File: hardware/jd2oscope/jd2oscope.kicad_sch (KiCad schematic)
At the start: 0 parts

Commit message: feat: kicad board dev
parts added, general framework established
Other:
- removed sheet Touchscreen
- removed sheet UserInteractionInterface
- added sheet ADCModule (ADCModule.kicad_sch)
- added sheet Touchscreen_LCD_Display (Touchscreen_LCD_Display.kicad_sch)
- added sheet buttonModule (buttonModule.kicad_sch)
- added sheet potentiometerModule (PotentiometerModule.kicad_sch)
- added sheet switchModule (switchModule.kicad_sch)
- note added: "(GPIO 18)"
- note added: "(GPIO 19)"
- note added: "(GPIO 23)"
- note added: "(any; GPIO 15)"
- note added: "(any; GPIO 2)"
- note added: "(any; GPIO 27)"
- note added: "(any; GPIO 5)"

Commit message: fix: pushing so people can edit!! (I think)
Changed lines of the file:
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@@
+		)
+	)
+	(hierarchical_label "screen_SDO"
+		(shape output)
+		(at 50.8 99.06 0)
+		(effects
+			(font
+				(size 1.27 1.27)
+			)
+			(justify left)
+		)
+	)
+	(hierarchical_label "5V"
+		(shape input)
+		(at 30.48 127 270)
+		(effects
+			(font
+				(size 1.27 1.27)
+			)
+			(justify right)
+		)
+	)
+	(hierarchical_label "screen_CS"
+		(shape input)
+		(at 50.8 83.82 0)
+		(effects
+			(font
+				(size 1.27 1.27)
+			)
+			(justify left)
+		)
+	)
+	(hierarchical_label "3.3V"
+		(shape input)
+		(at 33.02 127 270)
+		(effects
+			(font
+				(size 1.27 1.27)
+			)
+			(justify right)
+		)
+	)
+	(hierarchical_label "screen_SCK"
+		(shape input)
+		(at 50.8 95.25 0)
+		(effects
+			(font
+				(size 1.27 1.27)
+			)
+			(justify left)
+		)
+	)
+	(hierarchical_label "screen_T_IRQ"
+		(shape output)
+		(at 50.8 120.65 0)
+		(effects
+			(font
+				(size 1.27 1.27)
+			)
+			(justify left)
+		)
+	)
+	(hierarchical_label "screen_T_CS"
+		(shape input)
+		(at 50.8 109.22 0)
+		(effects
+			(font
+				(size 1.27 1.27)
+			)
+			(justify left)
+		)
+	)
+	(hierarchical_label "screen_T_DIN"
+		(shape input)
+		(at 50.8 113.03 0)
+		(effects
+			(font
+				(size 1.27 1.27)
+			)
+			(justify left)
+		)
+	)
+	(hierarchical_label "screen_T_DO"
+		(shape output)
+		(at 50.8 116.84 0)
+		(effects
+			(font
+				(size 1.27 1.27)
+			)
+			(justify left)
+		)
+	)
+	(hierarchical_label "screen_T_CLK"
+		(shape input)
+		(at 50.8 105.41 0)
+		(effects
+			(font
+				(size 1.27 1.27)
+			)
+			(justify left)
+		)
+	)
+	(hierarchical_label "screen_SDI"
+		(shape input)
+		(at 50.8 91.44 0)
+		(effects
+			(font
+				(size 1.27 1.27)
+			)
+			(justify left)
+		)
+	)
+	(hierarchical_label "screen_D{slash}C"
+		(shape input)
+		(at 50.8 87.63 0)
+		(effects
+			(font
+				(size 1.27 1.27)
+			)
+			(justify left)
+		)
+	)
+	(symbol
+		(lib_id "power:GND")
+		(at 50.8 125.73 90)
+		(unit 1)
+		(exclude_from_sim no)
+		(in_bom yes)
+		(on_board yes)
+		(dnp no)
+		(fields_autoplaced yes)
+		(property "Reference" "#PWR01"
+			(at 57.15 125.73 0)
+			(effects
+				(font
+					(size 1.27 1.27)
+				)
+				(hide yes)
+			)
+		)
+		(property "Value" "GND"
+			(at 54.61 125.7299 90)
+			(effects
+				(font
+					(size 1.27 1.27)
+				)
+				(justify right)
+			)
+		)
+		(property "Footprint" ""
+			(at 50.8 125.73 0)
+			(effects
+				(font
+					(size 1.27 1.27)
+				)
+				(hide yes)
+			)
+		)
+		(property "Datasheet" ""
+			(at 50.8 125.73 0)
+			(effects
+				(font
+					(size 1.27 1.27)
+				)
+				(hide yes)
+			)
+		)
+		(property "Description" "Power symbol creates a global label with name \"GND\" , ground"
+			(at 50.8 125.73 0)
+			(effects
+				(font
+					(size 1.27 1.27)
+				)
+				(hide yes)
+			)
+		)
+		(pin "1"
+		)
+		(instances
+			(project ""
+				(path "/eb18a3da-9fbf-4329-a814-1afab785c817"
+					(reference "#PWR01")
+					(unit 1)
+				)
+			)
 		)
 	)
@@
 	)
 	(sheet
-		(at 97.79 144.78)
-		(size 17.78 16.51)
+		(at 97.79 123.19)
+		(size 17.78 38.1)
 		(fields_autoplaced yes)
 		(stroke
@@
 		)
 		(property "Sheetname" "ESP32"
-			(at 97.79 144.0684 0)
-			(effects
-				(font
+			(at 97.79 122.4784 0)
+			(effects
+				(font

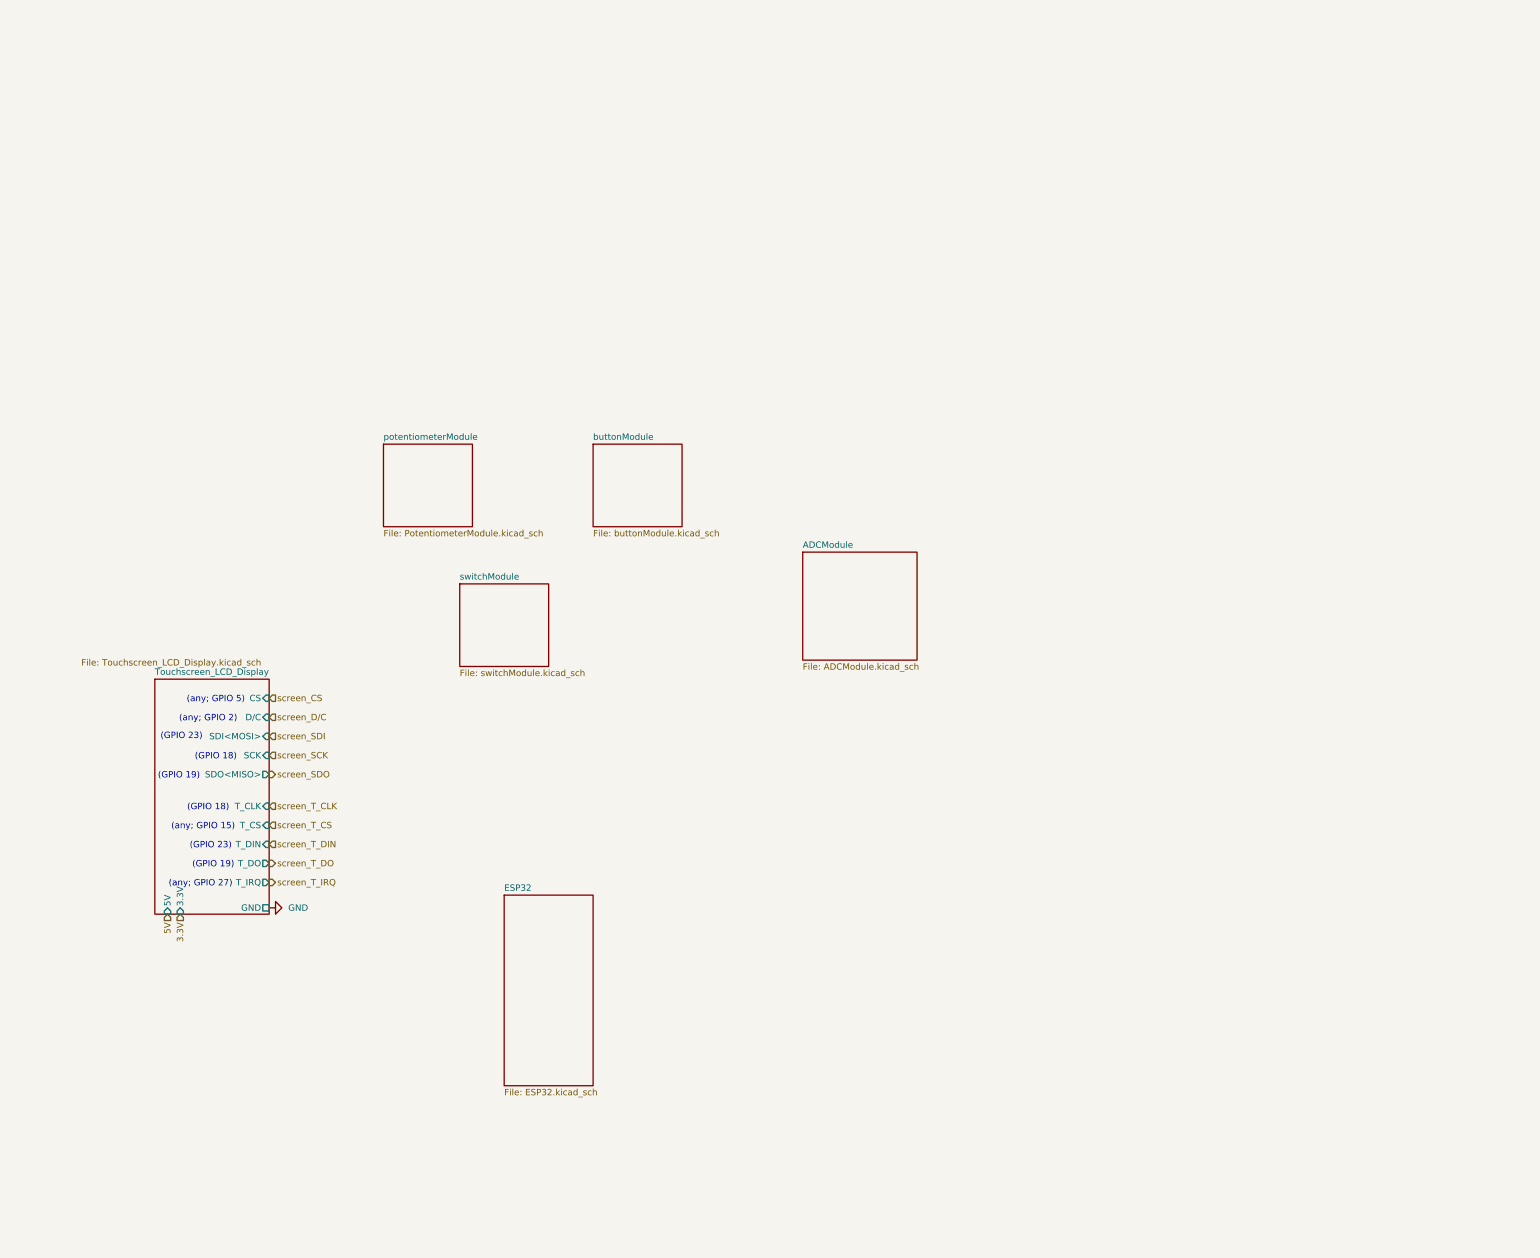
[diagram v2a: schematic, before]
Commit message: feat: screen implemented
alongside screen implementation, re-structured layout for schematics, and cleaned up SPI comm. conn.s; also implemented ADC module successfully (sans SPI section for it; that comes next)
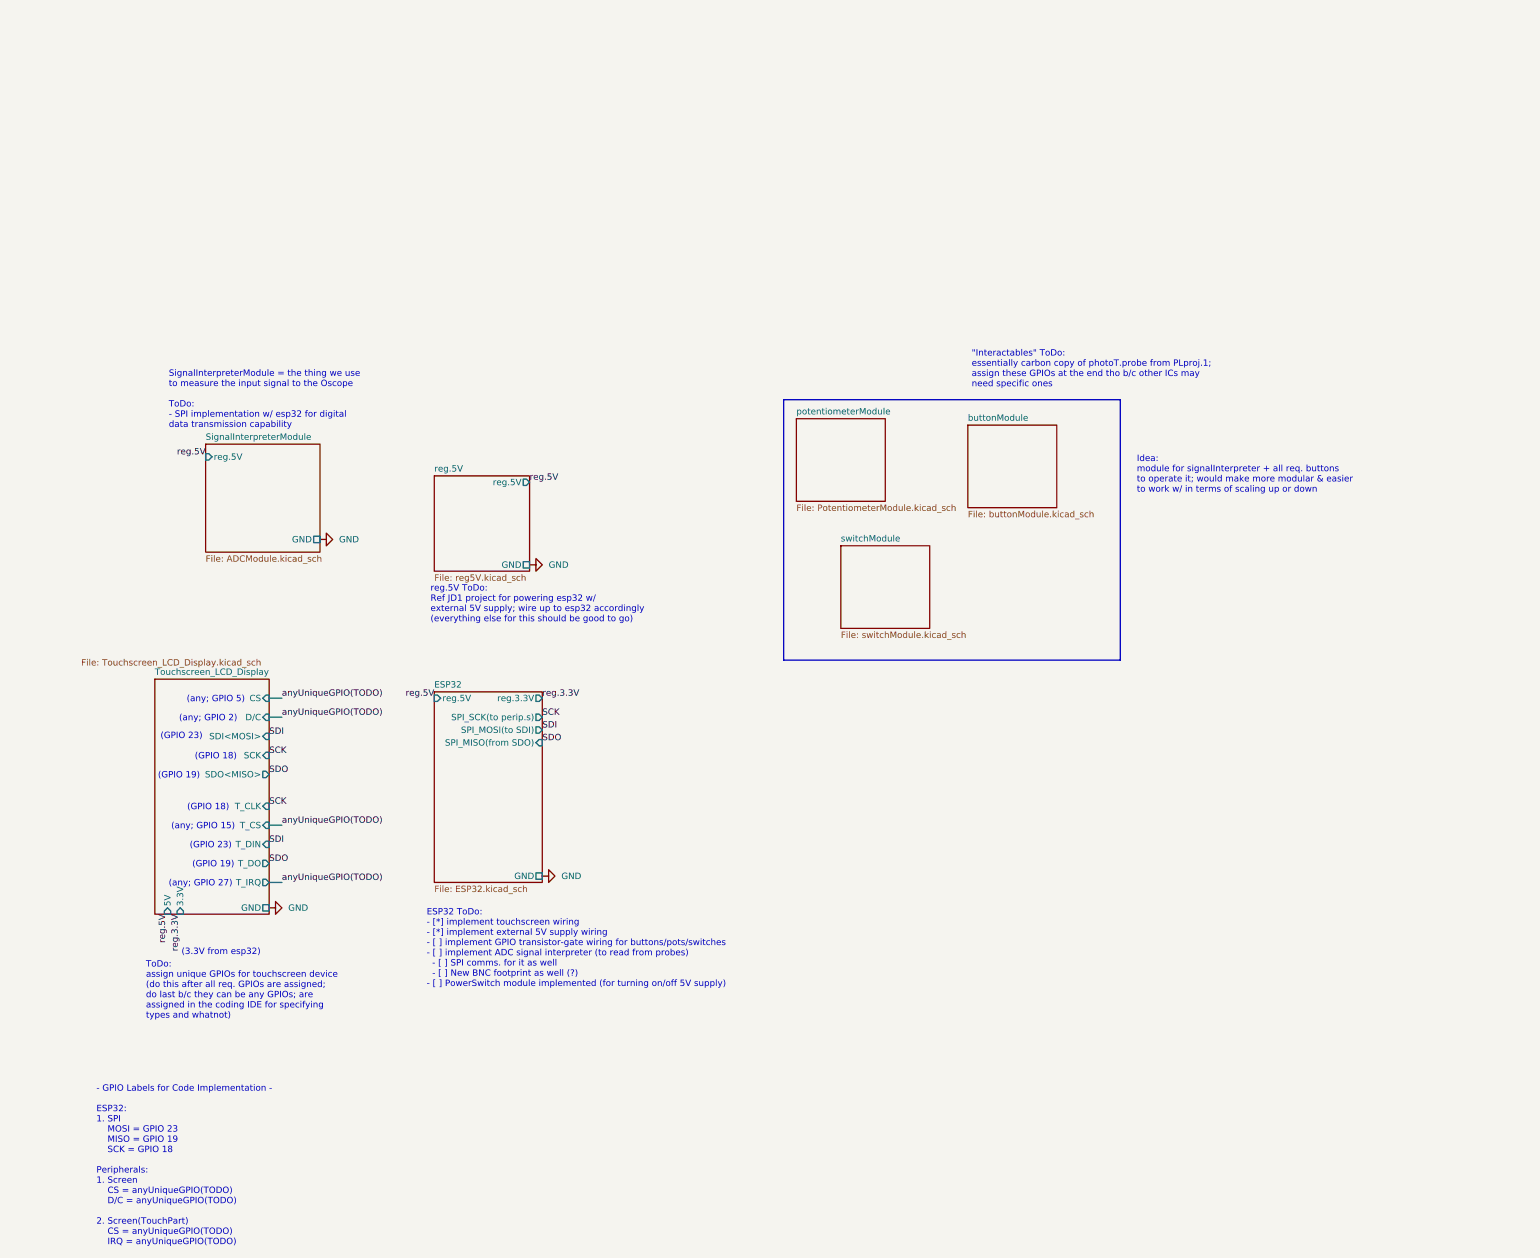
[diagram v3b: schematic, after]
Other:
- sheet ADCModule renamed SignalInterpreterModule
- added sheet reg.5V (reg5V.kicad_sch)
- sheet ESP32 ports: added GND, SPI_MISO(from SDO), SPI_MOSI(to SDI), SPI_SCK(to perip.s), reg.3.3V, reg.5V; removed none
- sheet SignalInterpreterModule ports: added GND, reg.5V; removed none
- note added: ""Interactables" ToDo: essentially carbon copy of photoT.probe from PLproj.1; assign these GPIOs at the end tho b/c other ICs may need specific ones"
- note added: "(3.3V from esp32)"
- note added: "- GPIO Labels for Code Implementation - ESP32: 1. SPI MOSI = GPIO 23 MISO = GPIO 19 SCK = GPIO 18 Peripherals: 1. Screen CS = anyUniqueGPIO(TODO) D/C = anyUniqueGPIO(TODO) 2. Screen(TouchPart) CS = anyUniqueGPIO(TODO) IRQ = anyUniqueGPIO(TODO)"
- note added: "ESP32 ToDo: - [*] implement touchscreen wiring - [*] implement external 5V supply wiring - [ ] implement GPIO transistor-gate wiring for buttons/pots/switches - [ ] implement ADC signal interpreter (to read from probes) - [ ] SPI comms. for it as well - [ ] New BNC footprint as well (?) - [ ] PowerSwitch module implemented (for turning on/off 5V supply)"
- note added: "Idea: module for signalInterpreter + all req. buttons to operate it; would make more modular & easier to work w/ in terms of scaling up or down"
- note added: "SignalInterpreterModule = the thing we use to measure the input signal to the Oscope ToDo: - SPI implementation w/ esp32 for digital data transmission capability"
- note added: "ToDo: assign unique GPIOs for touchscreen device (do this after all req. GPIOs are assigned; do last b/c they can be any GPIOs; are assigned in the coding IDE for specifying types and whatnot)"
- note added: "reg.5V ToDo: Ref JD1 project for powering esp32 w/ external 5V supply; wire up to esp32 accordingly (everything else for this should be good to go)"

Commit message: feat: lot of progress
added decoupling caps, implemented a lot more of the comm. protocol stuffs, updated BNC connector to updated version, added more notes for GPIO pin I/O for future code implementation, lot of other stuff too (frankly can't remember all of it lol); I commit here b/c want to back up progress b/4 I go get smth to eat ;)
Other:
- sheet reg.5V renamed 5V_Regulator
- removed sheet switchModule
- sheet SignalInterpreterModule ports: added ADC_CONVST, ADC_CS, ADC_EOC/INT, ADC_SCK, ADC_SDI, ADC_SDO; removed none
- sheet buttonModule ports: added GND, GPIOpin; removed none
- sheet potentiometerModule ports: added GND, POT_WIPER, reg.3.3V; removed none
- note added: "- GPIO Labels for Code Implementation - ESP32: 1. SPI MOSI = GPIO 23 MISO = GPIO 19 SCK = GPIO 18 Peripherals: 1. Screen(Display) S_CS = anyUniqueGPIO(TODO) D/C = anyUniqueGPIO(TODO) 2. Screen(Touchscreen Function) T_CS = anyUniqueGPIO(TODO) IRQ = anyUniqueGPIO(TODO) 3. ADC #1 ADC1_CS = anyUniqueGPIO(TODO) ADC1_CONVST = anyUniqueGPIO(TODO) ADC1_EOC/INT = anyUniqueGPIO(TODO) 4. ADC #2 ADC2_CS = an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"
- note added: "ESP32 Remaining Pinout ToDo: add arbitrary GPIO pins for all req. unique connections"
- note added: "ESP32 ToDo: - [*] implement touchscreen wiring - [*] implement 5V_Regulator - [*] PowerSwitch module between regulator output & reg.5V (for toggling reg.5V to all dependent perip.s (i.e. turning device on/off) - [ ] modules completed for: - [*] pot.s - [*] buttons - [ ] created "signalInterfaceModule"; has all req. buttons/pot.s to fully control 1x signal (like a "package" that has everything we 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"
- note added: "How many buttons & pot.s needed per "signal module"? - [ ] after determining, build signal module - [ ] try out hierarchecal pcb setup too(?) - compatability should be fine (?)"
- note added: "Remaining GPIOs: - [ ] for each of the potentiometers & buttons Helpful Note: - for GPIO groupings do this (ex): " Peripherals: SignalModule1: ADC1: ADC1_CS = (...) Button1 = (...) SignalModule2: (...) " ^Effectively, one "module" for e/a signal input; group e/a as a separate peripheral"
- note added: "SignalInterpreterModule = the module we use to measure a BNC input signal to the Oscope"
- note added: "ToDo: assign unique GPIOs for screen & TS perip.s (do this after all req. GPIOs are assigned; do last b/c they can be any GPIOs; are assigned in the coding IDE for specifying types and whatnot)"
- note removed: ""Interactables" ToDo: essentially carbon copy of photoT.probe from PLproj.1; assign these GPIOs at the end tho b/c other ICs may need specific ones"
- note removed: "(3.3V from esp32)"
- note removed: "- GPIO Labels for Code Implementation - ESP32: 1. SPI MOSI = GPIO 23 MISO = GPIO 19 SCK = GPIO 18 Peripherals: 1. Screen CS = anyUniqueGPIO(TODO) D/C = anyUniqueGPIO(TODO) 2. Screen(TouchPart) CS = anyUniqueGPIO(TODO) IRQ = anyUniqueGPIO(TODO)"
- note removed: "ESP32 ToDo: - [*] implement touchscreen wiring - [*] implement external 5V supply wiring - [ ] implement GPIO transistor-gate wiring for buttons/pots/switches - [ ] implement ADC signal interpreter (to read from probes) - [ ] SPI comms. for it as well - [ ] New BNC footprint as well (?) - [ ] PowerSwitch module implemented (for turning on/off 5V supply)"
- note removed: "Idea: module for signalInterpreter + all req. buttons to operate it; would make more modular & easier to work w/ in terms of scaling up or down"
- note removed: "SignalInterpreterModule = the thing we use to measure the input signal to the Oscope ToDo: - SPI implementation w/ esp32 for digital data transmission capability"
- note removed: "ToDo: assign unique GPIOs for touchscreen device (do this after all req. GPIOs are assigned; do last b/c they can be any GPIOs; are assigned in the coding IDE for specifying types and whatnot)"
- note removed: "reg.5V ToDo: Ref JD1 project for powering esp32 w/ external 5V supply; wire up to esp32 accordingly (everything else for this should be good to go)"

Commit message: feat: more stuff added
yep
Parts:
- added C11, C12, C13: 0.1u, Capacitor_SMD:C_0603_1608Metric_Pad1.08x0.95mm_HandSolder, symbol Device:C
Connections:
- net GND: now also C11.1, C12.1, C13.1
- net reg.3.3V: now also C13.2
- net reg.5V: now also C11.2, C12.2
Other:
- note added: "Next up: combine SignalInterpreterModule + buttonModule + potentiometerModule to make the signalInterfaceModule!"
- note added: "Note: wroom32 already has onboard decopling cap for reg.3.3V (no need to add!)"

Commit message: feat: finished schematics
I think! Subject to change tho! for now though at least, I think they look clean asf hah~
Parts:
- removed C11: 0.1u, Capacitor_SMD:C_0603_1608Metric_Pad1.08x0.95mm_HandSolder, symbol Device:C
- added C1: 0.1u, Capacitor_SMD:C_0603_1608Metric_Pad1.08x0.95mm_HandSolder, symbol Device:C
- added U1: ESP32-DEVKITC-32D, digikey-footprints:MODULE_ESP32-DEVKITC-32D, symbol ESP32-DEVKITC-32D:ESP32-DEVKITC-32D
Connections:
- net GND: now also C1.1, U1.J2-14 (GND1), U1.J3-1 (GND3), U1.J3-7 (GND2)
- net SCK: now also U1.J3-9 (IO18)
- net SDI: now also U1.J3-2 (IO23)
- net SDO: now also U1.J3-8 (IO19)
- net reg.3.3V: now also U1.J2-1 (3V3)
- net reg.5V: now also C1.2, U1.J2-19 (EXT_5V)
- new net GPIO:ADC1_CONVST: U1.J2-11 (IO27)
- new net GPIO:ADC1_CS: U1.J2-12 (IO14)
- new net GPIO:ADC1_EOC/INT: U1.J2-10 (IO26)
- new net GPIO:ADC2_CONVST: U1.J3-3 (IO22)
- new net GPIO:ADC2_CS: U1.J3-6 (IO21)
- new net GPIO:ADC2_EOC/INT: U1.J2-13 (IO12)
- new net GPIO:ampScale_wiper: U1.J2-8 (IO33)
- new net GPIO:screen_CS: U1.J3-10 (IO5)
- new net GPIO:screen_D/C: U1.J3-13 (IO4)
- new net GPIO:signal1_ampShiftWiper: U1.J2-5 (IO34)
- new net GPIO:signal1_timeShiftWiper: U1.J2-6 (IO35)
- new net GPIO:signal1_toggleBttn: U1.J3-12 (IO16)
- new net GPIO:signal2_ampShiftWiper: U1.J2-3 (SENSOR_VP)
- new net GPIO:signal2_timeShiftWiper: U1.J2-4 (SENSOR_VN)
- new net GPIO:signal2_toggleBttn: U1.J3-11 (IO17)
- new net GPIO:timeScale_wiper: U1.J2-7 (IO32)
- new net GPIO:touch_CS: U1.J3-16 (IO15)
- new net GPIO:touch_IRQ: U1.J2-9 (IO25)
- new net GPIO:triggerBttn: U1.J2-15 (IO13)
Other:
- removed sheet ESP32
- removed sheet SignalInterpreterModule
- removed sheet buttonModule
- removed sheet potentiometerModule
- added sheet SignalInterfaces (signalInterfaces.kicad_sch)
- note added: "- GPIO Labels for Code Implementation - ESP32: 1. SPI MOSI = GPIO 23 (IO23) // General I/O, Hardware VSPI MOSI MISO = GPIO 19 (IO19) // General I/O, Hardware VSPI MISO SCK = GPIO 18 (IO18) // General I/O, Hardware VSPI SCK Peripherals: 1. Screen(Display) screen_CS = GPIO 5 (IO5) // General I/O screen_D/C = GPIO 4 (IO4) // General I/O 2. Screen(Touchscreen Function) touch_CS = GPIO 15 (IO15) // St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"
- note added: "ESP32 ToDo: - [*] implement touchscreen wiring - [*] implement 5V_Regulator - [*] PowerSwitch module between regulator output & reg.5V (for toggling reg.5V to all dependent perip.s (i.e. turning device on/off) - [*] modules completed for: - [*] pot.s - [*] buttons - [*] created "signalInterfaceModule"; has all req. buttons/pot.s to fully control 1x signal (like a "package" that has everything we 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"
- note removed: "- GPIO Labels for Code Implementation - ESP32: 1. SPI MOSI = GPIO 23 MISO = GPIO 19 SCK = GPIO 18 Peripherals: 1. Screen(Display) S_CS = anyUniqueGPIO(TODO) D/C = anyUniqueGPIO(TODO) 2. Screen(Touchscreen Function) T_CS = anyUniqueGPIO(TODO) IRQ = anyUniqueGPIO(TODO) 3. ADC #1 ADC1_CS = anyUniqueGPIO(TODO) ADC1_CONVST = anyUniqueGPIO(TODO) ADC1_EOC/INT = anyUniqueGPIO(TODO) 4. ADC #2 ADC2_CS = an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"
- note removed: "ESP32 Remaining Pinout ToDo: add arbitrary GPIO pins for all req. unique connections"
- note removed: "ESP32 ToDo: - [*] implement touchscreen wiring - [*] implement 5V_Regulator - [*] PowerSwitch module between regulator output & reg.5V (for toggling reg.5V to all dependent perip.s (i.e. turning device on/off) - [ ] modules completed for: - [*] pot.s - [*] buttons - [ ] created "signalInterfaceModule"; has all req. buttons/pot.s to fully control 1x signal (like a "package" that has everything we 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"
- note removed: "How many buttons & pot.s needed per "signal module"? - [ ] after determining, build signal module - [ ] try out hierarchecal pcb setup too(?) - compatability should be fine (?)"
- note removed: "Next up: combine SignalInterpreterModule + buttonModule + potentiometerModule to make the signalInterfaceModule!"
- note removed: "Remaining GPIOs: - [ ] for each of the potentiometers & buttons Helpful Note: - for GPIO groupings do this (ex): " Peripherals: SignalModule1: ADC1: ADC1_CS = (...) Button1 = (...) SignalModule2: (...) " ^Effectively, one "module" for e/a signal input; group e/a as a separate peripheral"
- note removed: "SignalInterpreterModule = the module we use to measure a BNC input signal to the Oscope"
- note removed: "ToDo: assign unique GPIOs for screen & TS perip.s (do this after all req. GPIOs are assigned; do last b/c they can be any GPIOs; are assigned in the coding IDE for specifying types and whatnot)"
- moved on the sheet: C12, C13
